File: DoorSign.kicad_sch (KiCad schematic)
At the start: 37 parts, among them J1 Wall, J2 Taster, J3 Taster-LED, U1 Pico, U2 PC817, U3 LM2575-5.0BT

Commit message: Ignores
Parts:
- C1, C10: footprint Capacitor_THT:CP_Axial_L11.0mm_D8.0mm_P15.00mm_Horizontal -> Capacitor_THT:CP_Radial_D12.5mm_P5.00mm
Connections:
- net at R4.2, U2.4: now also U1.1 (GPIO0); no longer U1.21 (GPIO16)
- net at D2.4 (DIN): now also U1.2 (GPIO1); no longer U1.22 (GPIO17)
- net at R1.2, R2.2: now also U1.31 (GPIO26_ADC0); no longer U1.29 (GPIO22)

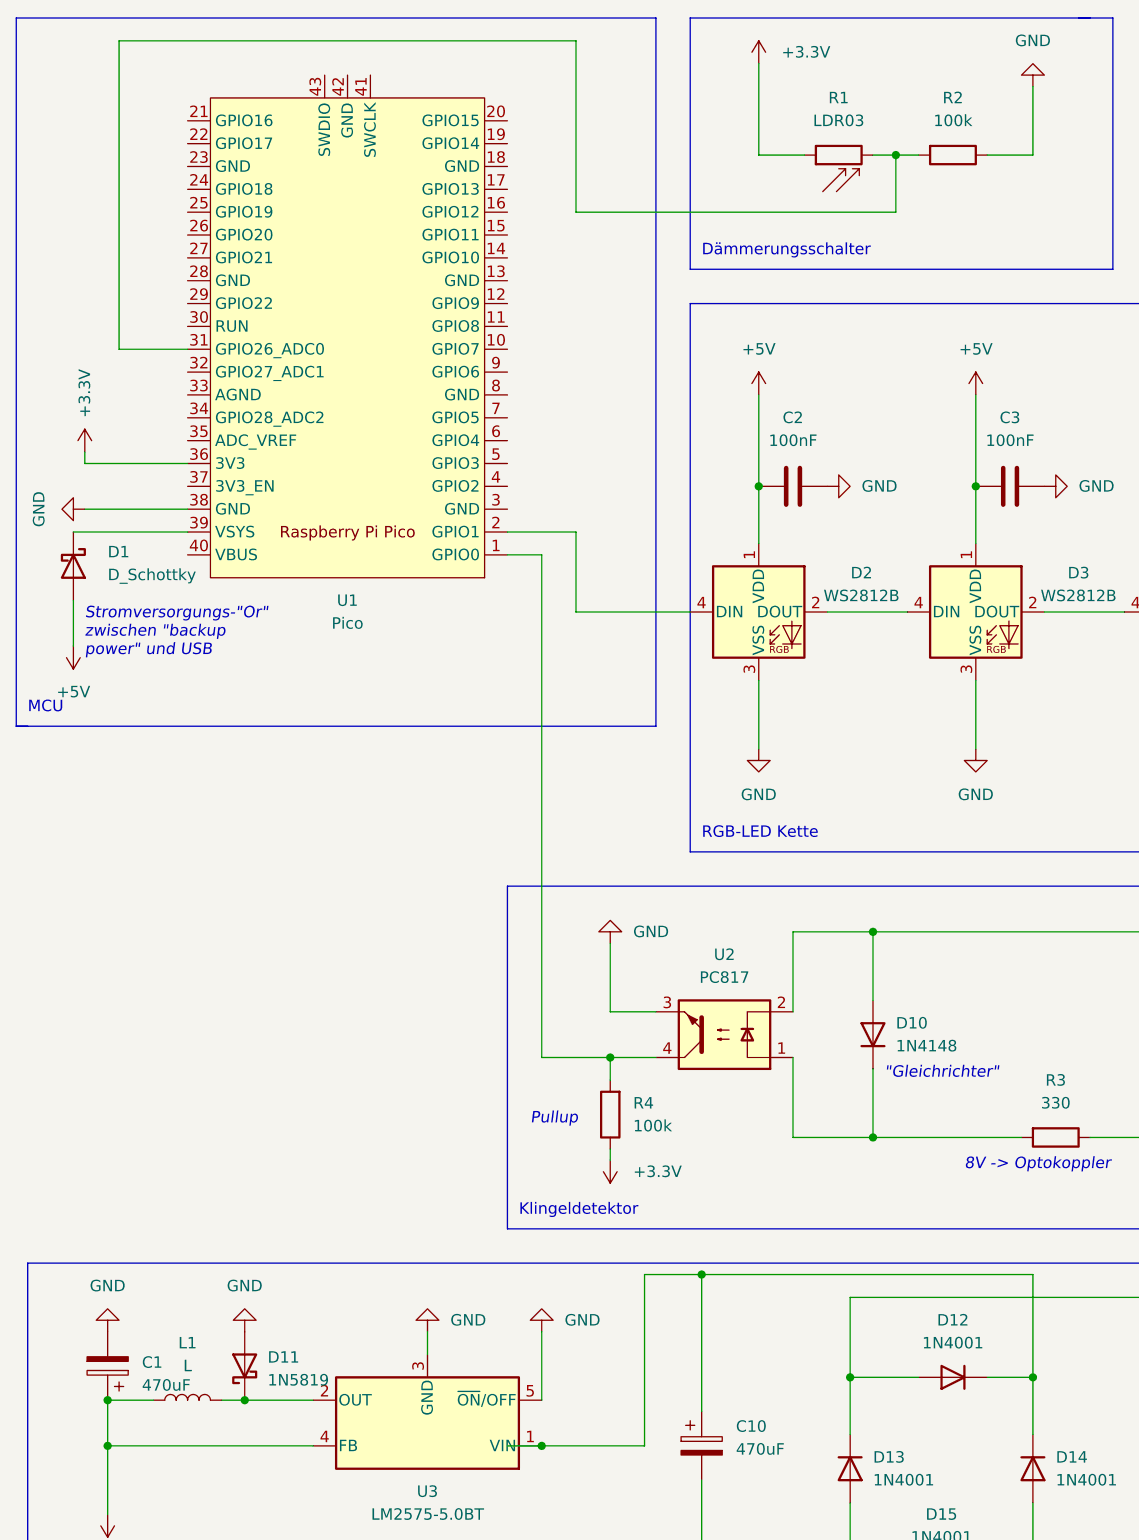
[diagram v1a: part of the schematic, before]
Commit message: Added BOM and partial schematics
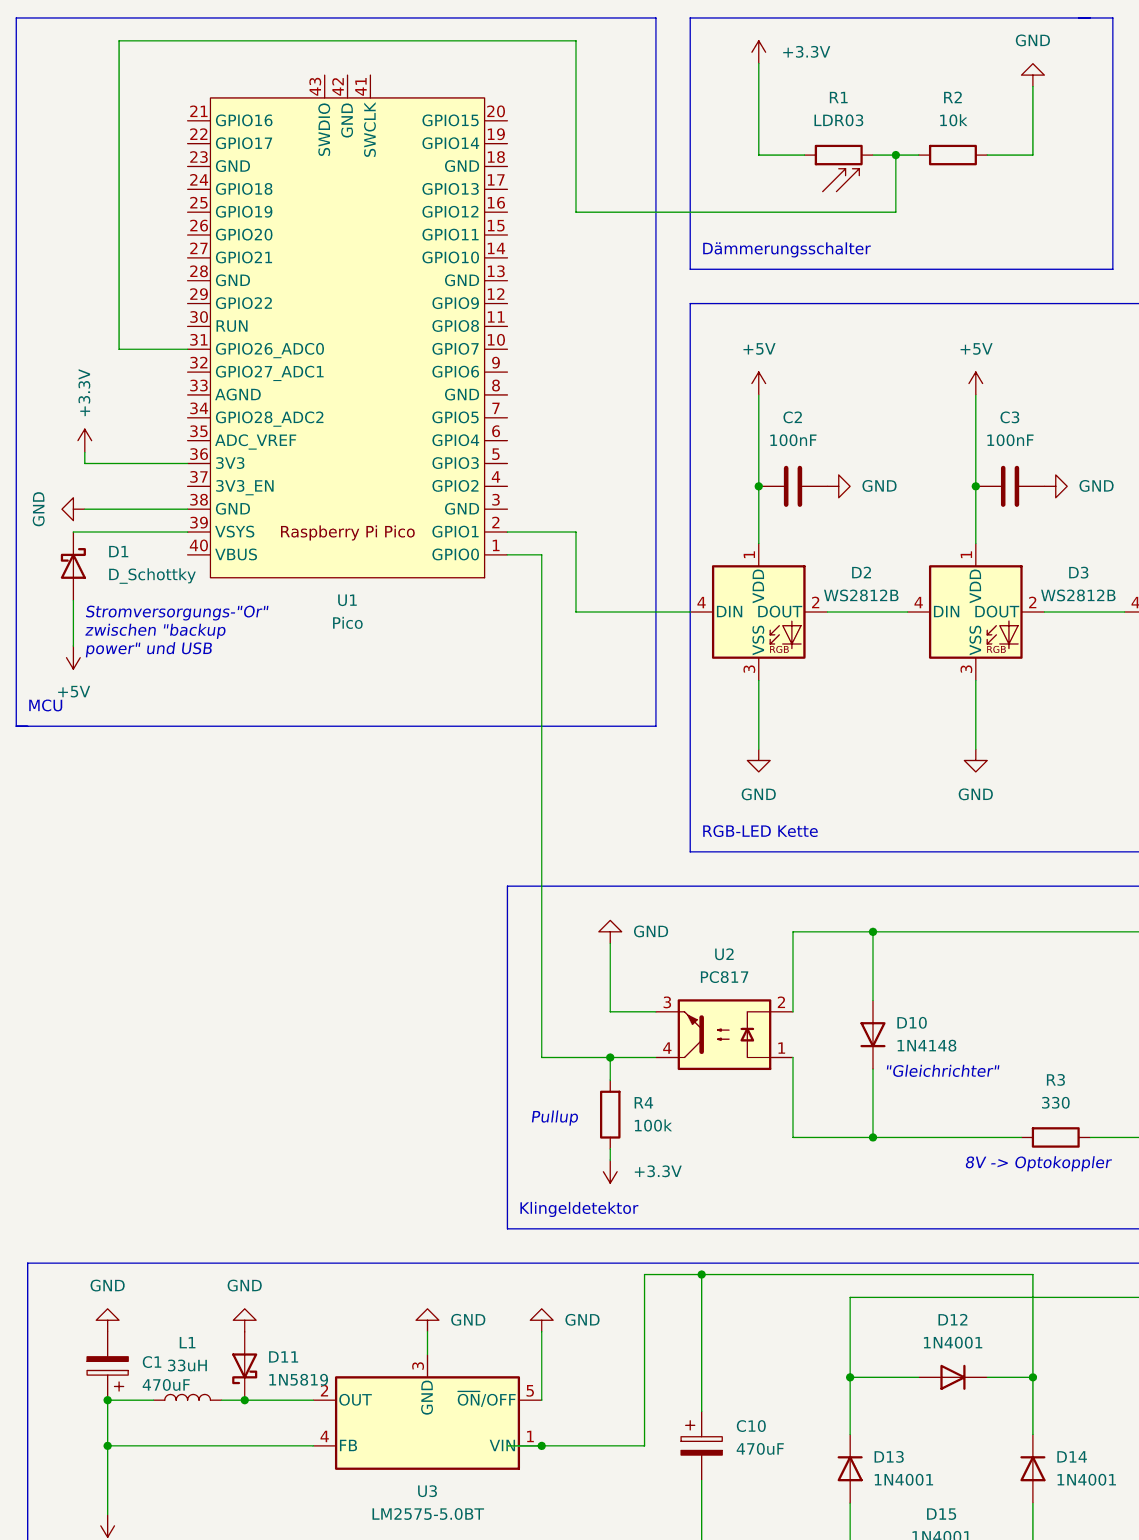
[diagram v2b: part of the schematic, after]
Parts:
- L1: value L -> 33uH; footprint Inductor_THT:L_Axial_L5.0mm_D3.6mm_P10.00mm_Horizontal_Murata_BL01RN1A2A2 -> Inductor_THT:L_Radial_D12.5mm_P7.00mm_Fastron_09HCP
- R2: value 100k -> 10k
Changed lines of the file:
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@@
     (in_bom yes) (on_board yes) (fields_autoplaced)
     (property "Reference" "R2" (id 0) (at 118.11 25.4 90))
-    (property "Value" "100k" (id 1) (at 118.11 27.94 90))
+    (property "Value" "10k" (id 1) (at 118.11 27.94 90))
     (property "Footprint" "Resistor_THT:R_Axial_DIN0207_L6.3mm_D2.5mm_P15.24mm_Horizontal" (id 2) (at 118.11 29.972 90)
       (effects (font (size 1.27 1.27)) hide)
@@
   (symbol (lib_id "power:+3.3V") (at 21.59 64.77 0) (unit 1)
     (in_bom yes) (on_board yes) (fields_autoplaced)
-    (property "Reference" "#PWR?" (id 0) (at 21.59 68.58 0)
+    (property "Reference" "#PWR0103" (id 0) (at 21.59 68.58 0)
       (effects (font (size 1.27 1.27)) hide)
     )
@@
     (in_bom yes) (on_board yes) (fields_autoplaced)
     (property "Reference" "L1" (id 0) (at 33.02 163.83 90))
-    (property "Value" "L" (id 1) (at 33.02 166.37 90))
-    (property "Footprint" "Inductor_THT:L_Axial_L5.0mm_D3.6mm_P10.00mm_Horizontal_Murata_BL01RN1A2A2" (id 2) (at 33.02 170.18 0)
+    (property "Value" "33uH" (id 1) (at 33.02 166.37 90))
+    (property "Footprint" "Inductor_THT:L_Radial_D12.5mm_P7.00mm_Fastron_09HCP" (id 2) (at 33.02 170.18 0)
       (effects (font (size 1.27 1.27)) hide)
     )
@@
   (symbol (lib_id "power:GND") (at 21.59 71.12 270) (unit 1)
     (in_bom yes) (on_board yes)
-    (property "Reference" "#PWR?" (id 0) (at 15.24 71.12 0)
+    (property "Reference" "#PWR0104" (id 0) (at 15.24 71.12 0)
       (effects (font (size 1.27 1.27)) hide)
     )
@@
   (symbol (lib_id "power:+5V") (at 20.32 86.36 180) (unit 1)
     (in_bom yes) (on_board yes) (fields_autoplaced)
-    (property "Reference" "#PWR?" (id 0) (at 20.32 82.55 0)
+    (property "Reference" "#PWR0102" (id 0) (at 20.32 82.55 0)
       (effects (font (size 1.27 1.27)) hide)
     )
@@
       (reference "#PWR0101") (unit 1) (value "GND") (footprint "")
     )
+    (path "/fbd6210b-5b8a-4516-80a8-c494d3a8c4aa"
+      (reference "#PWR0102") (unit 1) (value "+5V") (footprint "")
+    )
     (path "/65d856af-455e-4370-a62a-86db4add8d1c"
-      (reference "#PWR?") (unit 1) (value "+3.3V") (footprint "")
+      (reference "#PWR0103") (unit 1) (value "+3.3V") (footprint "")
     )
     (path "/be68d9b0-e067-4146-aacb-5c8f1e16dfa5"
-      (reference "#PWR?") (unit 1) (value "GND") (footprint "")
-    )
-    (path "/fbd6210b-5b8a-4516-80a8-c494d3a8c4aa"
-      (reference "#PWR?") (unit 1) (value "+5V") (footprint "")
+      (reference "#PWR0104") (unit 1) (value "GND") (footprint "")
     )
     (path "/49927729-dc2e-4ac4-b7aa-0e4f2f15cd80"
@@
     )
     (path "/783c6bba-2eb3-40e4-977f-72194ec38619"
-      (reference "L1") (unit 1) (value "L") (footprint "Inductor_THT:L_Axial_L5.0mm_D3.6mm_P10.00mm_Horizontal_Murata_BL01RN1A2A2")
+      (reference "L1") (unit 1) (value "33uH") (footprint "Inductor_THT:L_Radial_D12.5mm_P7.00mm_Fastron_09HCP")
     )
     (path "/514b804b-34d2-4c7c-9e21-9eacc38ed900"
@@
     )
     (path "/3b8e2598-127e-44a4-92fc-765ea868e8bf"
-      (reference "R2") (unit 1) (value "100k") (footprint "Resistor_THT:R_Axial_DIN0207_L6.3mm_D2.5mm_P15.24mm_Horizontal")
+      (reference "R2") (unit 1) (value "10k") (footprint "Resistor_THT:R_Axial_DIN0207_L6.3mm_D2.5mm_P15.24mm_Horizontal")
     )
     (path "/dc669c4c-1e7c-430f-966e-aef9a17d07be"

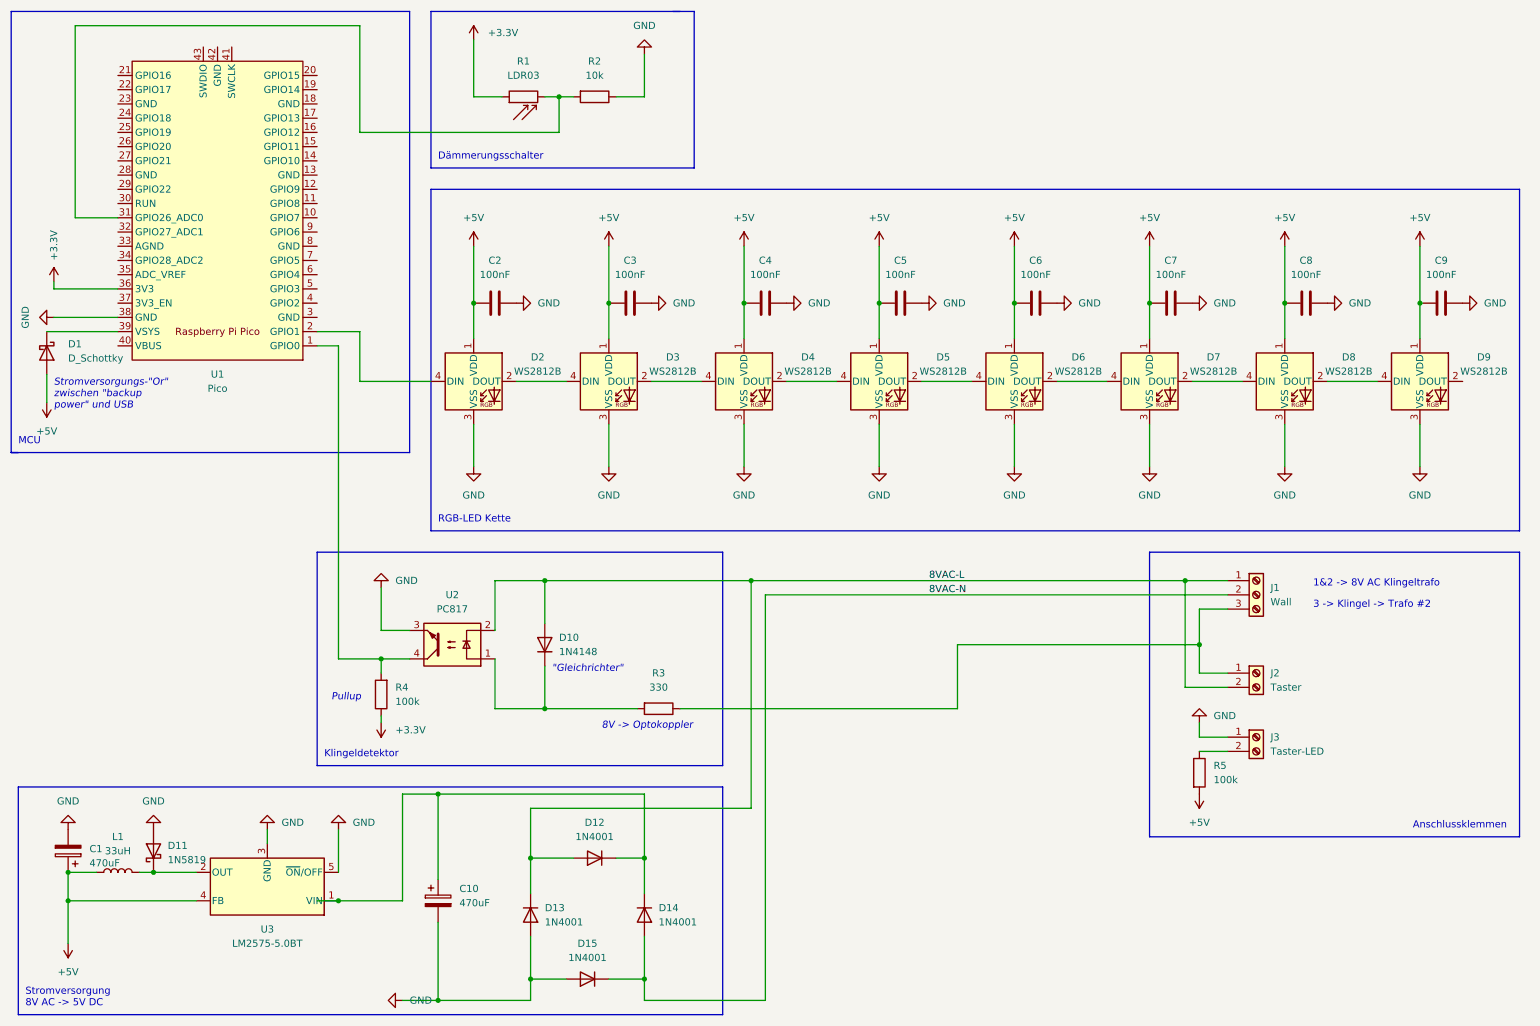
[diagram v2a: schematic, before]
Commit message: added jumper for optocoupler
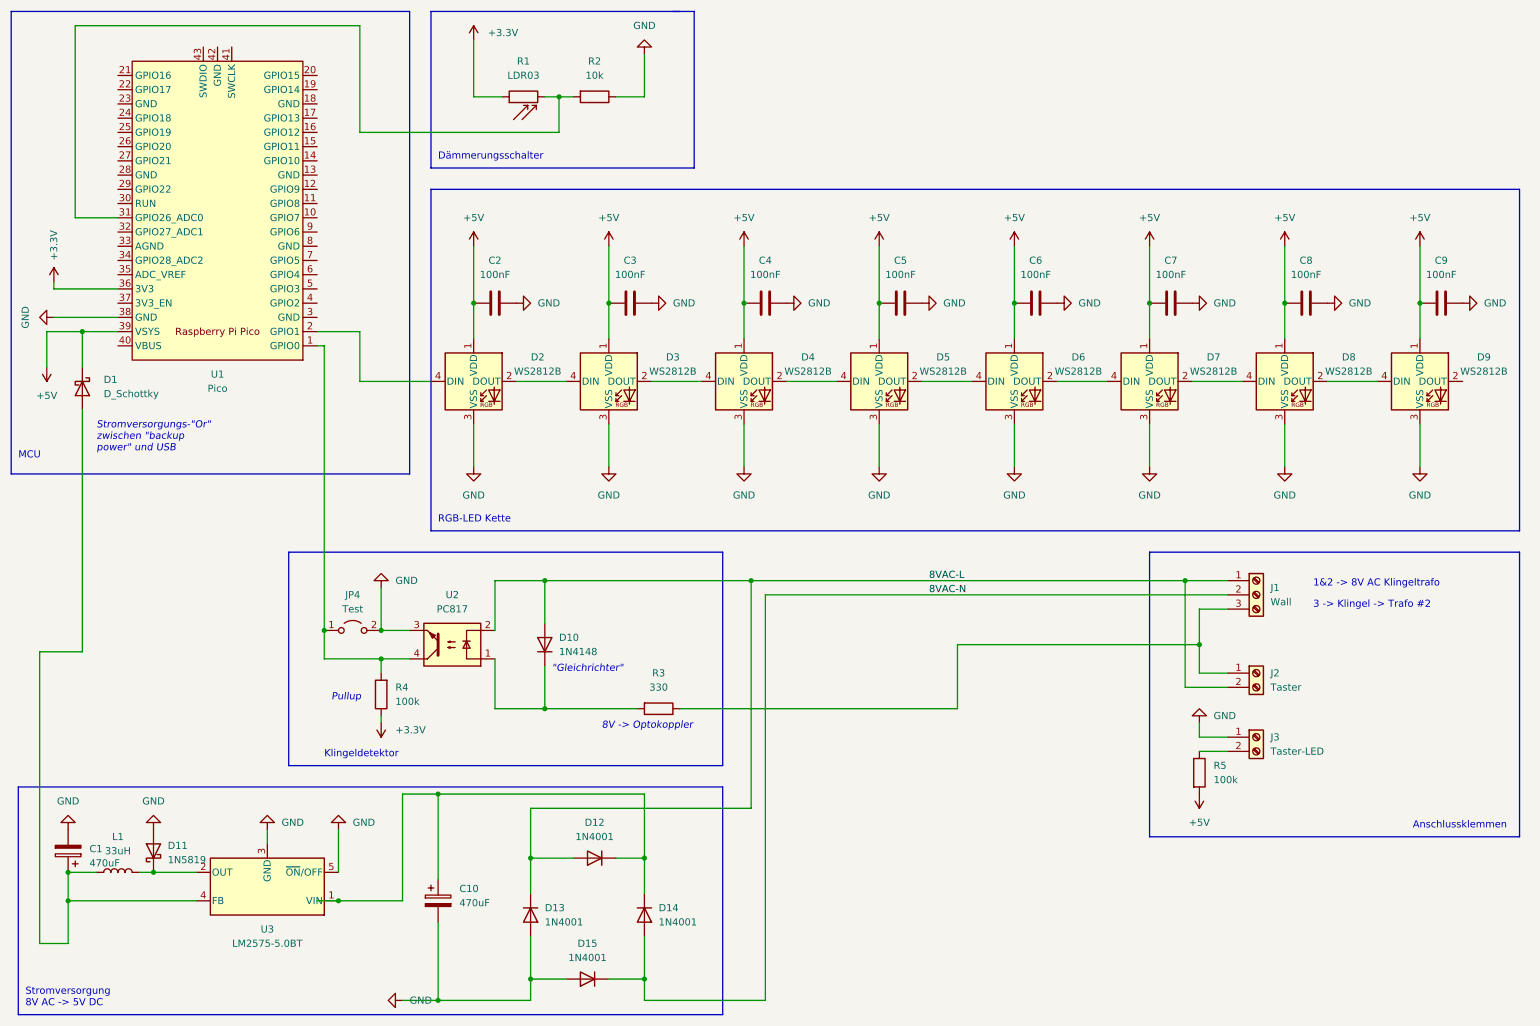
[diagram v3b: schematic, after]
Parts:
- added JP4: Test, TestPoint:TestPoint_2Pads_Pitch2.54mm_Drill0.8mm, symbol Jumper:Jumper_2_Open
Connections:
- net +5V: now also D1.1 (K), U1.39 (VSYS); no longer C1.1, D1.2 (A), L1.1, U3.4 (FB)
- net GND: now also JP4.2 (B)
- net at R4.2, U1.1 (GPIO0), U2.4: now also JP4.1 (A)
- new net: C1.1, D1.2 (A), L1.1, U3.4 (FB)
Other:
- moved on the sheet: D1
